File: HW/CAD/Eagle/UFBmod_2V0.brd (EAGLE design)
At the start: 98.4 x 89.5 mm, 192 parts, among them T0551 MMBT2222, U0501 MIDAS_MCCOG21605B6W-FPTLWI, U0601 MAX5217, U0701 AT86RF215-ZU, U0711 ASVTX-13-D-26.000MHZ-I05-T, U0811 PE4259, U0821 RFX1010, U0881 B39871B3440U410, U0911 FT232HL, U1101 TPS53353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

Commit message: HW - CAD/Eagle - update FPGA assignments
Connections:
- removed net FPGA_ROT_I: R1011.2
- removed net FPGA_ROT_P: R1013.2
- removed net FPGA_ROT_Q: R1012.2
- new net BOARD_ROTENC_I: JB2.22, R1011.2
- new net BOARD_ROTENC_PUSH: JB2.26, R1013.2
- new net BOARD_ROTENC_Q: JB2.24, R1012.2
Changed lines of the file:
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@@
 <wire x1="71.12" y1="87.63" x2="71.12" y2="86.375" width="0.1524" layer="1"/>
 </signal>
-<signal name="FPGA_ROT_I">
+<signal name="BOARD_ROTENC_I">
 <contactref element="R1011" pad="2"/>
+<contactref element="JB2" pad="22"/>
+<wire x1="33.67" y1="5.08" x2="48.63" y2="59.11" width="0" layer="19" extent="1-16"/>
 </signal>
-<signal name="FPGA_ROT_Q">
+<signal name="BOARD_ROTENC_Q">
 <contactref element="R1012" pad="2"/>
+<contactref element="JB2" pad="24"/>
+<wire x1="33.67" y1="10.16" x2="49.13" y2="59.11" width="0" layer="19" extent="1-16"/>
 </signal>
-<signal name="FPGA_ROT_P">
+<signal name="BOARD_ROTENC_PUSH">
 <contactref element="R1013" pad="2"/>
+<contactref element="JB2" pad="26"/>
+<wire x1="15.89" y1="10.16" x2="49.63" y2="59.11" width="0" layer="19" extent="1-16"/>
 </signal>
 <signal name="FPGA_ETH_TD_P" class="3">

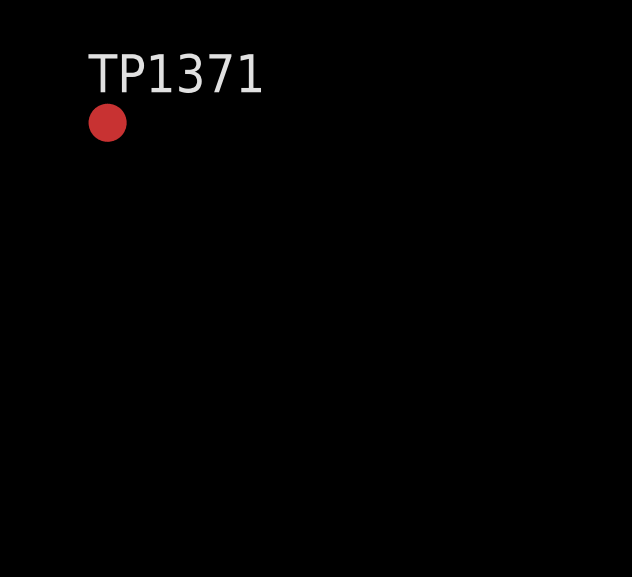
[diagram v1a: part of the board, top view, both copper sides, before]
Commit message: HW_2V0 - CAD/Eagle - RESET button added
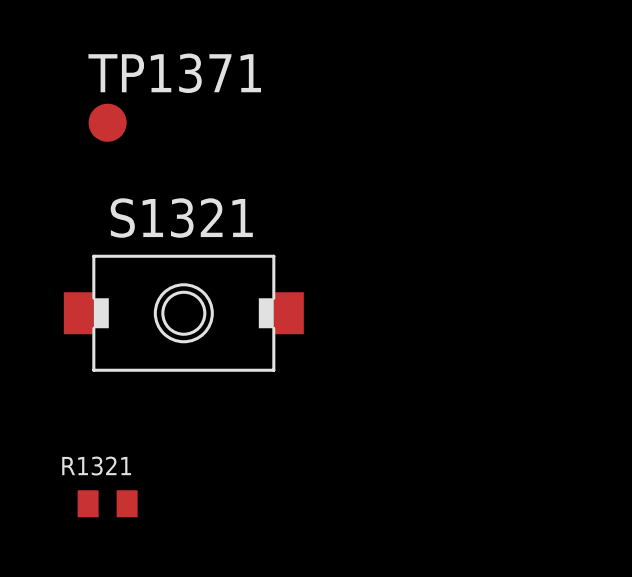
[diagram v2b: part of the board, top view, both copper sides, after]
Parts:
- added R1321: 100R, df4iah_rcl:R0402
- added S1321: KSR223G_SMD_1POL, df4iah_switch:KSR223G_SMD_1POL
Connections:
- new net FPGA_RESET: JB3.41, JB3.43, R1321.1
- new net FPGA_RESET_R: R1321.2, S1321.1
- net VCCIO13: now also S1321.2
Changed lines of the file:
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@@
 <attribute name="TP_SIGNAL_NAME" value="" x="-21.59" y="-27.94" size="0.6096" layer="27" ratio="20" display="off"/>
 </element>
+<element name="S1321" library="df4iah_switch" package="KSR223G_SMD_1POL" value="KSR223G_SMD_1POL" x="-19.05" y="-34.29"/>
+<element name="R1321" library="df4iah_rcl" package="R0402" value="100R" x="-21.59" y="-40.64"/>
 </elements>
 <signals>
@@
 <via x="44.1325" y="57.4675" extent="1-16" drill="0.3"/>
 <wire x1="44.1325" y1="57.4675" x2="44.1325" y2="56.37125" width="0.1524" layer="16"/>
+<contactref element="S1321" pad="2"/>
 <wire x1="44.13" y1="59.11" x2="43.63" y2="59.11" width="0" layer="19" extent="1-1"/>
+<wire x1="-15.55" y1="-34.29" x2="42.70375" y2="56.37125" width="0" layer="19" extent="1-16"/>
 </signal>
 <signal name="+2V5">
@@
 <contactref element="TP1371" pad="TP"/>
 </signal>
+<signal name="FPGA_RESET">
+<contactref element="JB3" pad="41"/>
+<contactref element="JB3" pad="43"/>
+<contactref element="R1321" pad="1"/>
+<wire x1="33.03" y1="48.21" x2="33.03" y2="47.71" width="0" layer="19" extent="1-1"/>
+<wire x1="-22.24" y1="-40.64" x2="33.03" y2="47.71" width="0" layer="19" extent="1-1"/>
+</signal>
+<signal name="FPGA_RESET_R">
+<contactref element="R1321" pad="2"/>
+<contactref element="S1321" pad="1"/>
+<wire x1="-22.55" y1="-34.29" x2="-20.94" y2="-40.64" width="0" layer="19" extent="1-1"/>
+</signal>
 </signals>

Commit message: HW_2V0 - CAD/Eagle - signal name change
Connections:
- net INIT_CALIB_COMPLETE renamed DDR3_INIT_CALIB_COMPLETE
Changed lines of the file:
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@@
 <contactref element="R0532" pad="1"/>
 </signal>
-<signal name="INIT_CALIB_COMPLETE">
+<signal name="DDR3_INIT_CALIB_COMPLETE">
 <contactref element="TP1371" pad="TP"/>
 </signal>

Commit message: HW_2V0 - CAD/Eagle - Ethernet Link-LED added
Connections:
- net FPGA_ETH_DA_G: now also JB2.18
- net FPGA_ETH_DA_Y: now also JB2.16
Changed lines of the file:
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@@
 <signal name="FPGA_ETH_DA_G">
 <contactref element="R1422" pad="1"/>
+<contactref element="JB2" pad="18"/>
+<wire x1="47.63" y1="59.11" x2="72.39" y2="53.99" width="0" layer="19" extent="1-16"/>
 </signal>
 <signal name="FPGA_ETH_DA_Y">
 <contactref element="R1421" pad="1"/>
+<contactref element="JB2" pad="16"/>
+<wire x1="47.13" y1="59.11" x2="72.39" y2="34.91" width="0" layer="19" extent="1-16"/>
 </signal>
 <signal name="TRX_RSTN_R">

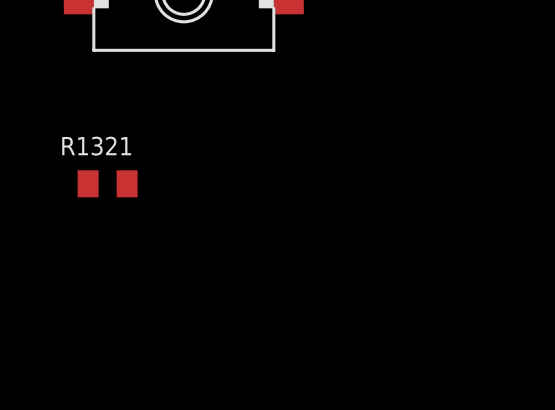
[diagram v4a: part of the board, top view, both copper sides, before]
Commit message: HW_2V0 - CAD/Eagle - connect TRX VC-TCXO 26MHz with FPGA
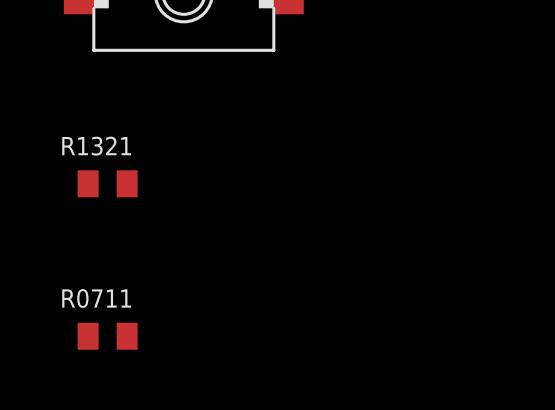
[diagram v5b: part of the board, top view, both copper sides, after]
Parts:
- added R0711: 100R, df4iah_rcl:R0402
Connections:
- new net TRX_CLKO_26MHZ_R: R0711.2, U0701.22
- new net TRX_CLK_26MHZ: JB2.52, R0711.1
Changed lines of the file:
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@@
 <element name="S1321" library="df4iah_switch" package="KSR223G_SMD_1POL" value="KSR223G_SMD_1POL" x="-19.05" y="-34.29"/>
 <element name="R1321" library="df4iah_rcl" package="R0402" value="100R" x="-21.59" y="-40.64"/>
+<element name="R0711" library="df4iah_rcl" package="R0402" value="100R" x="-21.59" y="-45.72"/>
 </elements>
 <signals>
@@
 <wire x1="-22.55" y1="-34.29" x2="-20.94" y2="-40.64" width="0" layer="19" extent="1-1"/>
 </signal>
+<signal name="TRX_CLKO_26MHZ_R">
+<contactref element="U0701" pad="22"/>
+<contactref element="R0711" pad="2"/>
+<wire x1="15.55" y1="38.89" x2="-20.94" y2="-45.72" width="0" layer="19" extent="1-1"/>
+</signal>
+<signal name="TRX_CLK_26MHZ">
+<contactref element="R0711" pad="1"/>
+<contactref element="JB2" pad="52"/>
+<wire x1="-22.24" y1="-45.72" x2="56.13" y2="59.11" width="0" layer="19" extent="1-1"/>
+</signal>
 </signals>

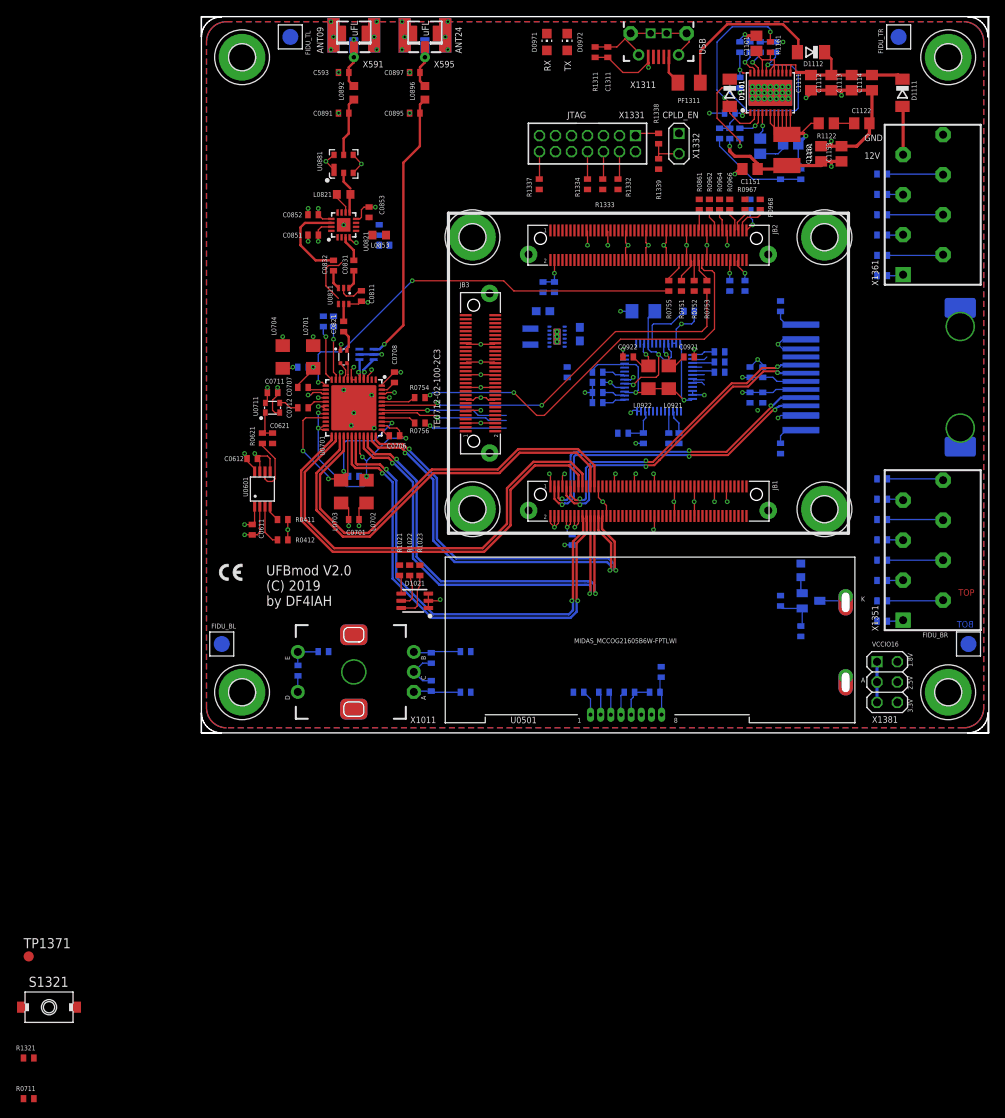
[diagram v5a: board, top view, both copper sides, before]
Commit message: HW_2V0 - CAD/Eagle - move all devices on the PCB area
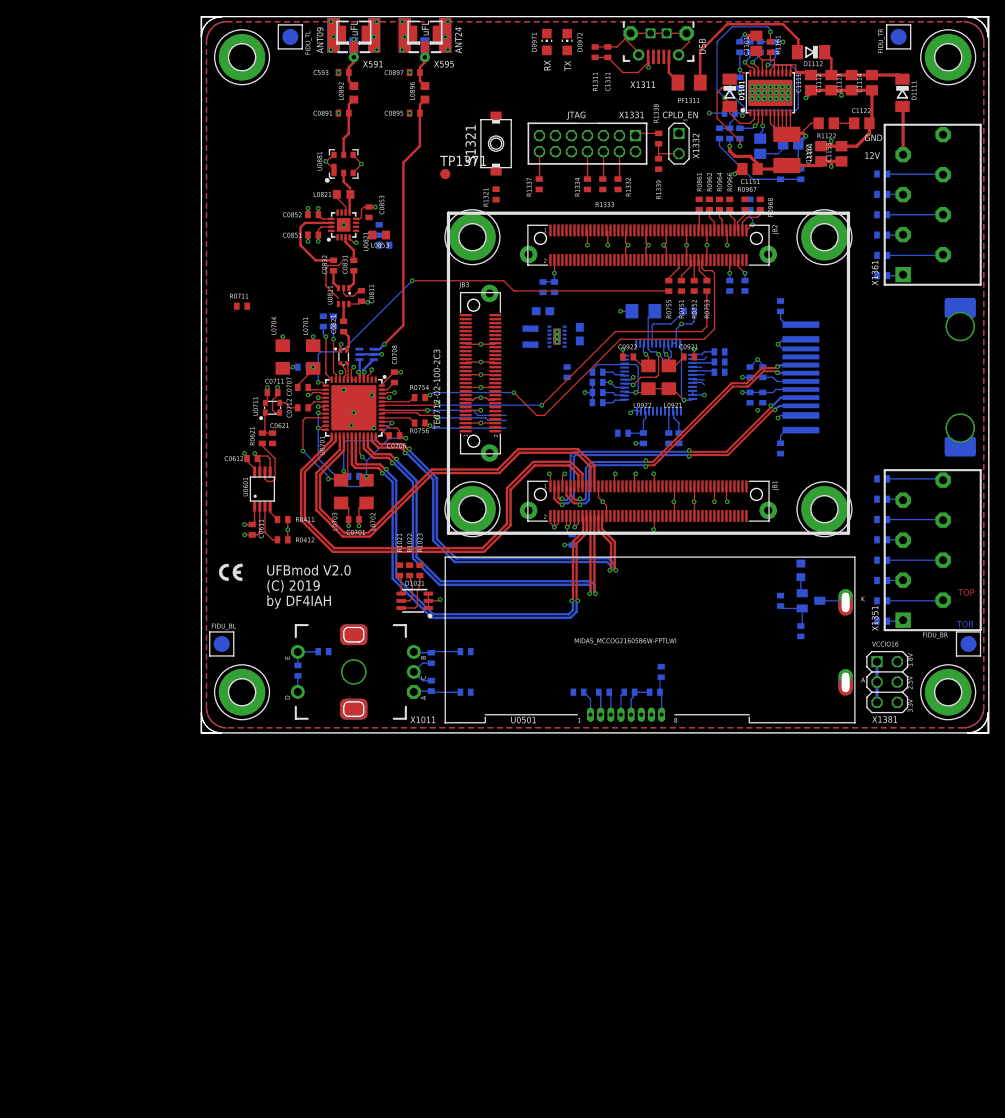
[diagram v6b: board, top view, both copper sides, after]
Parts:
- moved R1321 122.7 mm to (36.8, 67.3), turned to 90 degrees
- moved S1321 121.6 mm to (36.8, 73.7), turned to 90 degrees
- moved TP1371 110.8 mm to (30.5, 69.8)
- moved R0711 102.6 mm to (5.08, 53.3)
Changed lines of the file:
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@@
 <attribute name="VALUE" x="25.7175" y="40.3225" size="0.6096" layer="27" font="vector" ratio="10"/>
 </element>
-<element name="TP1371" library="df4iah_connector" package="B1,27" value="TPB1,27" x="-21.59" y="-27.94">
-<attribute name="TP_SIGNAL_NAME" value="" x="-21.59" y="-27.94" size="0.6096" layer="27" ratio="20" display="off"/>
+<element name="TP1371" library="df4iah_connector" package="B1,27" value="TPB1,27" x="30.48" y="69.85">
+<attribute name="TP_SIGNAL_NAME" value="" x="30.48" y="69.85" size="0.6096" layer="27" ratio="20" display="off"/>
 </element>
-<element name="S1321" library="df4iah_switch" package="KSR223G_SMD_1POL" value="KSR223G_SMD_1POL" x="-19.05" y="-34.29"/>
-<element name="R1321" library="df4iah_rcl" package="R0402" value="100R" x="-21.59" y="-40.64"/>
-<element name="R0711" library="df4iah_rcl" package="R0402" value="100R" x="-21.59" y="-45.72"/>
+<element name="S1321" library="df4iah_switch" package="KSR223G_SMD_1POL" value="KSR223G_SMD_1POL" x="36.83" y="73.66" rot="R90"/>
+<element name="R1321" library="df4iah_rcl" package="R0402" value="100R" x="36.83" y="67.31" rot="R90"/>
+<element name="R0711" library="df4iah_rcl" package="R0402" value="100R" x="5.08" y="53.34"/>
 </elements>
 <signals>
@@
 <contactref element="S1321" pad="2"/>
 <wire x1="44.13" y1="59.11" x2="43.63" y2="59.11" width="0" layer="19" extent="1-1"/>
-<wire x1="-15.55" y1="-34.29" x2="42.70375" y2="56.37125" width="0" layer="19" extent="1-16"/>
+<wire x1="36.83" y1="77.16" x2="42.70375" y2="56.37125" width="0" layer="19" extent="1-16"/>
 </signal>
 <signal name="+2V5">
@@
 <contactref element="R1321" pad="1"/>
 <wire x1="33.03" y1="48.21" x2="33.03" y2="47.71" width="0" layer="19" extent="1-1"/>
-<wire x1="-22.24" y1="-40.64" x2="33.03" y2="47.71" width="0" layer="19" extent="1-1"/>
+<wire x1="36.83" y1="66.66" x2="33.03" y2="47.71" width="0" layer="19" extent="1-1"/>
 </signal>
 <signal name="FPGA_RESET_R">
 <contactref element="R1321" pad="2"/>
 <contactref element="S1321" pad="1"/>
-<wire x1="-22.55" y1="-34.29" x2="-20.94" y2="-40.64" width="0" layer="19" extent="1-1"/>
+<wire x1="36.83" y1="70.16" x2="36.83" y2="67.96" width="0" layer="19" extent="1-1"/>
 </signal>
 <signal name="TRX_CLKO_26MHZ_R">
 <contactref element="U0701" pad="22"/>
 <contactref element="R0711" pad="2"/>
-<wire x1="15.55" y1="38.89" x2="-20.94" y2="-45.72" width="0" layer="19" extent="1-1"/>
+<wire x1="15.55" y1="38.89" x2="5.73" y2="53.34" width="0" layer="19" extent="1-1"/>
 </signal>
 <signal name="TRX_CLK_26MHZ">
 <contactref element="R0711" pad="1"/>
 <contactref element="JB2" pad="52"/>
-<wire x1="-22.24" y1="-45.72" x2="56.13" y2="59.11" width="0" layer="19" extent="1-1"/>
+<wire x1="4.43" y1="53.34" x2="56.13" y2="59.11" width="0" layer="19" extent="1-1"/>
 </signal>
 </signals>
